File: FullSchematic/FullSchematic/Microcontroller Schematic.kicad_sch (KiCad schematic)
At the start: 30 parts, among them J1 USB_B_Micro, J3 Conn_01x24_Socket, J4 Conn_01x24_Socket, U2 FT231XS, U3 24LC64

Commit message: completed and generated BOM
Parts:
- C4, C6, C7: Price $0.0685 -> 0.08; Price ( 1 board) 0.2055 -> 0.32; Price (5 boards) 1.0275 -> 1.6
- J1: JLCPCB Part # (none) -> C404969
- U3: JLCPCB Part # (none) -> C511260
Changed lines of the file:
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@@
+      (effects (font (size 1.27 1.27)) hide)
+    )
+    (property "JLCPCB Part #" "C404969" (at 130.81 58.42 0)
       (effects (font (size 1.27 1.27)) hide)
     )
@@
       (effects (font (size 1.27 1.27)) hide)
     )
-    (property "Price" "$0.0685" (at 114.3 86.36 0)
-      (effects (font (size 1.27 1.27)) hide)
-    )
-    (property "Price ( 1 board)" "0.2055" (at 114.3 86.36 0)
-      (effects (font (size 1.27 1.27)) hide)
-    )
-    (property "Price (5 boards)" "1.0275" (at 114.3 86.36 0)
+    (property "Price" "0.08" (at 114.3 86.36 0)
+      (effects (font (size 1.27 1.27)) hide)
+    )
+    (property "Price ( 1 board)" "0.32" (at 114.3 86.36 0)
+      (effects (font (size 1.27 1.27)) hide)
+    )
+    (property "Price (5 boards)" "1.6" (at 114.3 86.36 0)
       (effects (font (size 1.27 1.27)) hide)
     )
@@
     )
     (property "Price (5 boards)" "2.586" (at 63.5 57.15 0)
+      (effects (font (size 1.27 1.27)) hide)
+    )
+    (property "JLCPCB Part #" "C511260" (at 63.5 57.15 0)
       (effects (font (size 1.27 1.27)) hide)
     )
@@
       (effects (font (size 1.27 1.27)) hide)
     )
-    (property "Price" "$0.0685" (at 212.09 41.91 0)
-      (effects (font (size 1.27 1.27)) hide)
-    )
-    (property "Price ( 1 board)" "0.2055" (at 212.09 41.91 0)
-      (effects (font (size 1.27 1.27)) hide)
-    )
-    (property "Price (5 boards)" "1.0275" (at 212.09 41.91 0)
+    (property "Price" "0.08" (at 212.09 41.91 0)
+      (effects (font (size 1.27 1.27)) hide)
+    )
+    (property "Price ( 1 board)" "0.32" (at 212.09 41.91 0)
+      (effects (font (size 1.27 1.27)) hide)
+    )
+    (property "Price (5 boards)" "1.6" (at 212.09 41.91 0)
       (effects (font (size 1.27 1.27)) hide)
     )
@@
       (effects (font (size 1.27 1.27)) hide)
     )
-    (property "Price" "$0.0685" (at 125.73 86.36 0)
-      (effects (font (size 1.27 1.27)) hide)
-    )
-    (property "Price ( 1 board)" "0.2055" (at 125.73 86.36 0)
-      (effects (font (size 1.27 1.27)) hide)
-    )
-    (property "Price (5 boards)" "1.0275" (at 125.73 86.36 0)
-      (effects (font (size 1.27 1.27)) hide)
-    )
+    (property "Price" "0.08" (at 125.73 86.36 0)
+      (effects (font (size 1.27 1.27)) hide)
+    )
+    (property "Price ( 1 board)" "0.32" (at 125.73 86.36 0)
+      (effects (font (size 1.27 1.27)) hide)
+    )
+    (property "Price (5 boards)" "1.6" (at 125.73 86.36 0)
+      (effects (font (size 1.27 1.27)) hide)
+    )

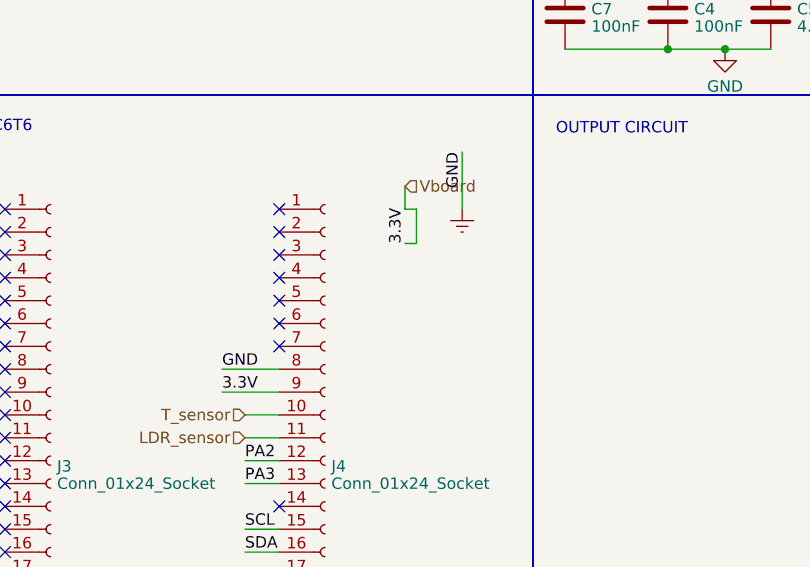
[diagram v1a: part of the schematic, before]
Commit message: added power flags
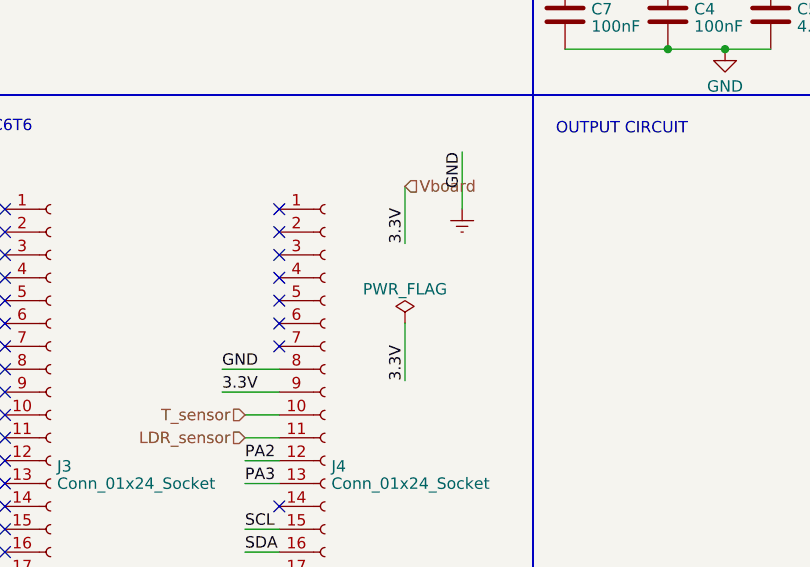
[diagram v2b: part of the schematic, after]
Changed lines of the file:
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@@
-    (stroke (width 0) (type default))
-  )
-  (wire (pts (xy 96.52 111.76) (xy 97.79 111.76))
     (stroke (width 0) (type default))
   )
@@
     (stroke (width 0) (type default))
   )
+  (wire (pts (xy 96.52 120.65) (xy 96.52 127))
+    (stroke (width 0) (type default))
+  )
   (wire (pts (xy 125.73 82.55) (xy 137.16 82.55))
     (stroke (width 0) (type default))
   )
-  (wire (pts (xy 96.52 105.41) (xy 96.52 107.95))
+  (wire (pts (xy 96.52 105.41) (xy 96.52 111.76))
     (stroke (width 0) (type default))
   )
@@
     (stroke (width 0) (type default))
   )
-  (wire (pts (xy 97.79 107.95) (xy 97.79 111.76))
-    (stroke (width 0) (type default))
-  )
   (wire (pts (xy 193.04 40.64) (xy 193.04 44.45))
     (stroke (width 0) (type default))
@@
   )
   (wire (pts (xy 102.87 101.6) (xy 102.87 107.95))
-    (stroke (width 0) (type default))
-  )
-  (wire (pts (xy 96.52 107.95) (xy 97.79 107.95))
     (stroke (width 0) (type default))
   )
@@
   )
   (label "PA2" (at 78.74 135.89 0) (fields_autoplaced)
+    (effects (font (size 1.27 1.27)) (justify left bottom))
+  )
+  (label "3.3V" (at 96.52 127 90) (fields_autoplaced)
     (effects (font (size 1.27 1.27)) (justify left bottom))
   )
@@
         )
       )
+    )
+  )
+  (symbol (lib_id "power:PWR_FLAG") (at 96.52 120.65 0) (unit 1)
+    (in_bom yes) (on_board yes) (dnp no) (fields_autoplaced)
+    (property "Reference" "#FLG03" (at 96.52 118.745 0)
+      (effects (font (size 1.27 1.27)) hide)
+    )
+    (property "Value" "PWR_FLAG" (at 96.52 116.84 0)
+      (effects (font (size 1.27 1.27)))
+    )
+    (property "Footprint" "" (at 96.52 120.65 0)
+      (effects (font (size 1.27 1.27)) hide)
+    )
+    (property "Datasheet" "~" (at 96.52 120.65 0)
+      (effects (font (size 1.27 1.27)) hide)
+    )
+    (pin "1")
+    (instances
+      (project "FullSchematic"
+        (path "/5dd86611-a33d-45ee-946c-01c599f30b12/5d08bf44-0550-4275-b6e8-e4566a125a74"
+          (reference "#FLG03") (unit 1)
+        )
+      )

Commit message: Corrected errors
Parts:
- removed C2: 47pF, symbol Device:C
- removed C3: 10nF, symbol Device:C
- removed C4, C6, C7: 100nF, symbol Device:C
- removed C5: 4.7uF, symbol Device:C
- removed R4, R5: 27R, symbol Device:R_US
- removed R7: 4700, symbol Device:R_US
- removed R8: 10k, symbol Device:R_US
- removed TP7: TestPoint, symbol Connector:TestPoint
- removed U2: FT231XS, Package_SO:SSOP-20_3.9x8.7mm_P0.635mm, symbol Interface_USB:FT231XS
- added U2: CH340C, Package_SO:SOIC-16_3.9x9.9mm_P1.27mm, symbol Interface_USB:CH340C
- C1: value 47pF -> 100nF; JLCPCB Part # C105622 -> C24497; Price $0.0447 -> 0.08; Price ( 1 board) 0.0894 -> 0.32; Price (5 boards) 0.447 -> 1.6
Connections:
- net Earth: now also U2.1 (GND)
- net PA2: now also U2.2 (TXD)
- net PA3: now also U2.3 (RXD)
- net Vboard: now also C1.1, U2.16 (VCC), U2.4 (V3)
- net +5V: now reaches J1.1 (VBUS)
- net at J1.2 (D-): now also U2.6 (UD-)
- net at J1.3 (D+): now also U2.5 (UD+); no longer C1.1
- no-connect marks 42 -> 39
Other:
- moved on the sheet: J1
